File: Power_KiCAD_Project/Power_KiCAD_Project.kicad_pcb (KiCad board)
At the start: 4 copper layers, 80 x 87.2 mm, 73 parts, among them IC1 STM32L562VET6Q, J1 XT60-M, J2 XT60-M, J3 XT60-M, J4 XT60-M, J5 XT60-M, J6 PJ-102AH, J7 L717SDC37P1ACH4F, Q1 CSD17501Q5A, Q2 BSS84PH6327XTSA2, Q3 CSD17501Q5A, SW1 Reboot, U1 MCP9808_MSOP, U2 MCP9808_MSOP, U3 BQ76920PW, U4 LM2678SX-5.0/NOPB, U5 LM2678SX-3.3/NOPB, Y1 Crystal

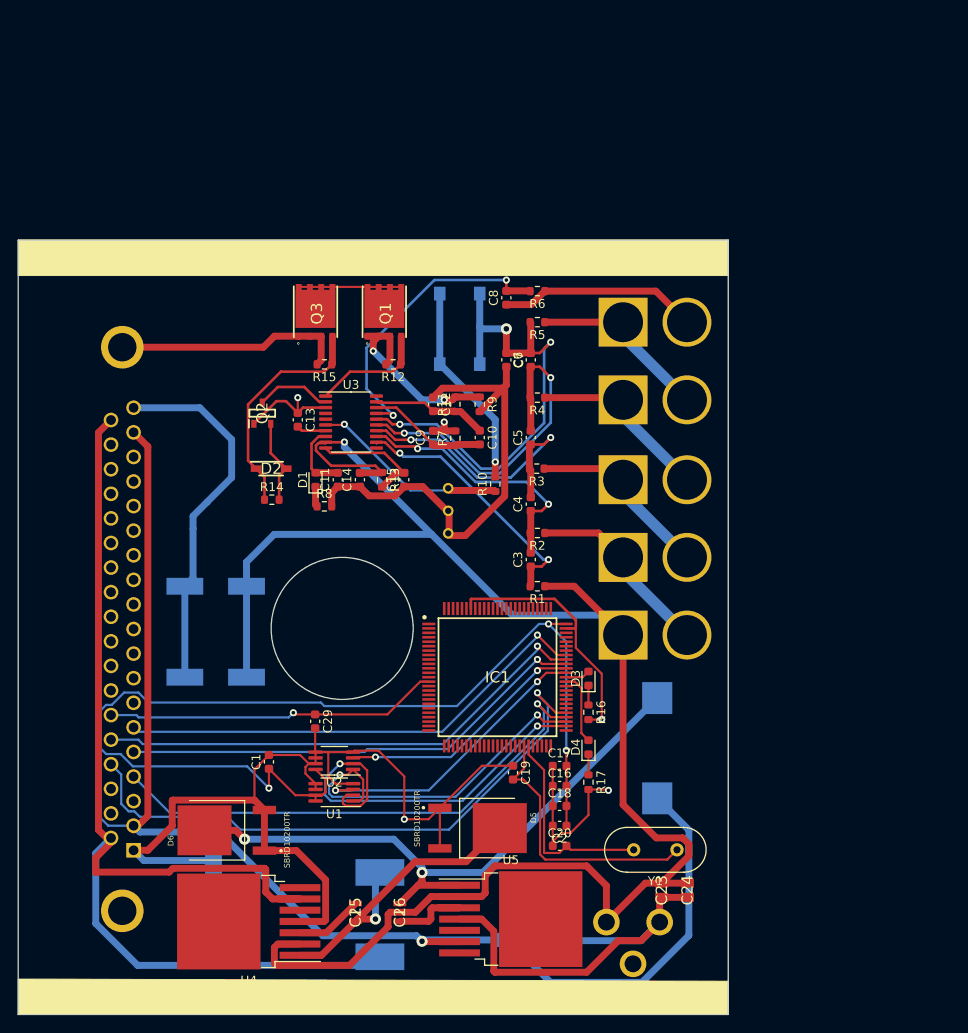
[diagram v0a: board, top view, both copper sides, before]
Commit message: Changes to PCB
re did the pcb and added a "switch"
basically its just an xt60 connector in series with the other ones that needs to be shorted for the board to get power
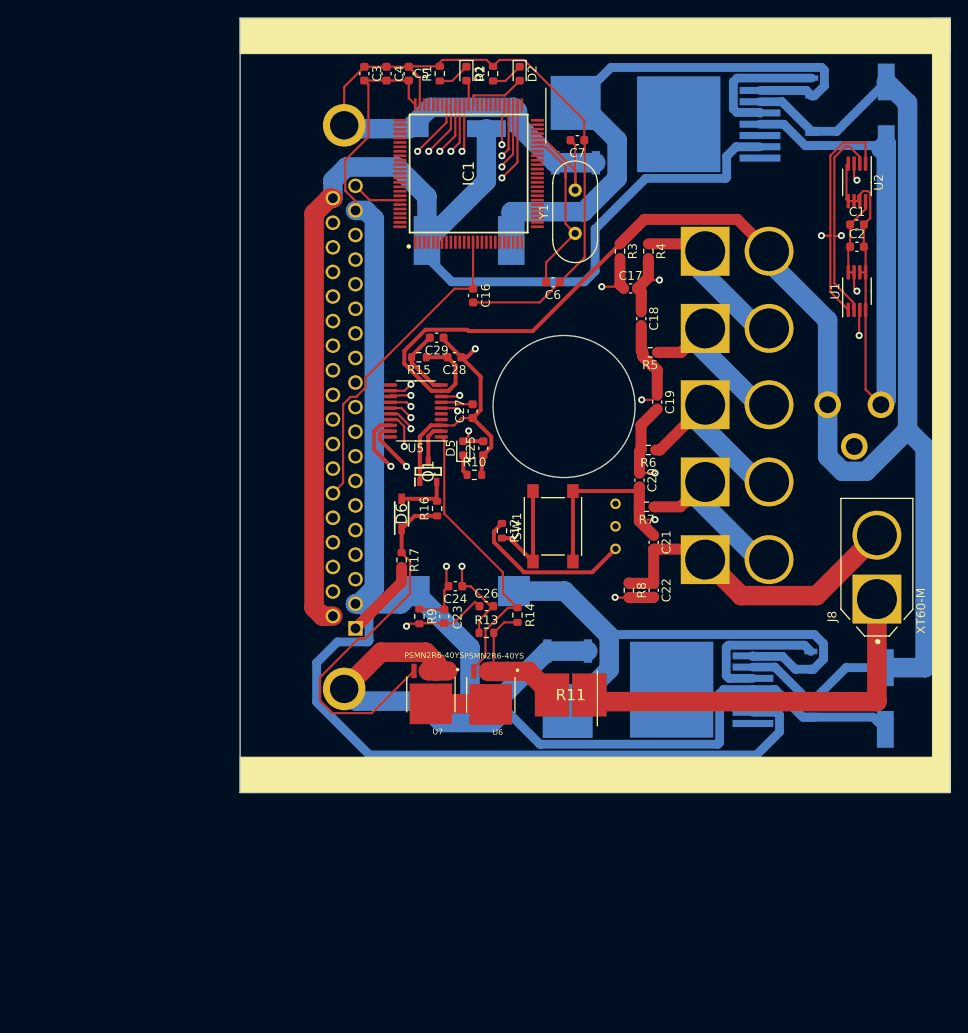
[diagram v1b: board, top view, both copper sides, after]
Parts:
- removed Q2: BSS84PH6327XTSA2, SamacSys_Parts:SOT95P240X110-3N
- removed Q3: CSD17501Q5A, SamacSys_Parts:Q5A
- added J8: XT60-M, XT60-M:AMASS_XT60-M, F.Cu at (171.8, 99.6)
- added U6: PSMN2R6-40YS, TO127P600X120-5N:TO127P600X120-5N, F.Cu at (128.2, 114.0)
- added U7: PSMN2R6-40YS, TO127P600X120-5N:TO127P600X120-5N, F.Cu at (121.5, 113.9)
- C10: value 0.1μF -> C0805C104M5RACTU; footprint Capacitor_SMD:C_0603_1608Metric -> SamacSys_Parts:CAPC2012X88N; moved to B.Cu
- C11: value 4.7μF -> C0805C104M5RACTU; footprint Capacitor_SMD:C_0603_1608Metric -> SamacSys_Parts:CAPC2012X88N; moved to B.Cu
- C12: value 0.1μF -> CGA4C2C0G1H103J060AA; footprint Capacitor_SMD:C_0603_1608Metric -> SamacSys_Parts:CAPC2012X75N; moved to B.Cu
- C13: value 1μF -> CGA4C2C0G1H103J060AA; footprint Capacitor_SMD:C_0603_1608Metric -> SamacSys_Parts:CAPC2012X75N; moved to B.Cu
- C14: value 1μF -> 16SVP330M; footprint Capacitor_SMD:C_0603_1608Metric -> SamacSys_Parts:16SVF1000M; moved to B.Cu
- C15: value 10μF -> 6SVPC330M; footprint Capacitor_SMD:C_0603_1608Metric -> SamacSys_Parts:16SVF180M; moved to B.Cu
- C16: value 1uF -> 100nF
- C17, C18: value 100nF -> 1μF
- C19, C20: value 30pF -> 1μF
- C21, C22: value 35SVPF82M -> 1μF; footprint SamacSys_Parts:16SVPT560M -> Capacitor_SMD:C_0603_1608Metric; moved to F.Cu
- C23, C24: value C0805C104M5RACTU -> 0.1μF; footprint SamacSys_Parts:CAPC2012X88N -> Capacitor_SMD:C_0603_1608Metric
- C25: value CGA4C2C0G1H103J060AA -> 4.7μF; footprint SamacSys_Parts:CAPC2012X75N -> Capacitor_SMD:C_0603_1608Metric
- C26: value CGA4C2C0G1H103J060AA -> 0.1μF; footprint SamacSys_Parts:CAPC2012X75N -> Capacitor_SMD:C_0603_1608Metric
- C27: value 16SVP330M -> 1μF; footprint SamacSys_Parts:16SVF1000M -> Capacitor_SMD:C_0603_1608Metric; moved to F.Cu
- C28: value 6SVPC330M -> 1μF; footprint SamacSys_Parts:16SVF180M -> Capacitor_SMD:C_0603_1608Metric; moved to F.Cu
- C29: value 100nF -> 10μF
- C3: value 1μF -> 1uF
- C4, C5: value 1μF -> 100nF
- C6, C7: value 1μF -> 30pF
- C8: value 1μF -> 35SVPF82M; footprint Capacitor_SMD:C_0603_1608Metric -> SamacSys_Parts:16SVPT560M; moved to B.Cu
- C9: value 0.1μF -> 35SVPF82M; footprint Capacitor_SMD:C_0603_1608Metric -> SamacSys_Parts:16SVPT560M; moved to B.Cu
- D1: value LED -> GREEN
- D2: value 1N4148W-7-F -> RED; footprint SamacSys_Parts:SOD3716X145N -> LED_SMD:LED_0603_1608Metric
- D3: value GREEN -> SBRD10200TR; footprint LED_SMD:LED_0603_1608Metric -> SBRD10200TR:DPAK228P1005X240-4N; moved to B.Cu
- D4: value RED -> SBRD10200TR; footprint LED_SMD:LED_0603_1608Metric -> SBRD10200TR:DPAK228P1005X240-4N; moved to B.Cu
- D5: value SBRD10200TR -> LED; footprint SBRD10200TR:DPAK228P1005X240-4N -> LED_SMD:LED_0603_1608Metric
- D6: value SBRD10200TR -> 1N4148W-7-F; footprint SBRD10200TR:DPAK228P1005X240-4N -> SamacSys_Parts:SOD3716X145N
- Q1: value CSD17501Q5A -> BSS84PH6327XTSA2; footprint SamacSys_Parts:Q5A -> SamacSys_Parts:SOT95P240X110-3N
- R1, R2: value 100Ω -> 1k5Ω
- R10: value 10kΩ -> 1k5Ω
- R11: value 100Ω -> WSHP28185L000FEA; footprint Resistor_SMD:R_0603_1608Metric -> SamacSys_Parts:RESC7146X175N
- R12: value 1MΩ -> 10kΩ
- R15: value 1MΩ -> 100Ω
- R16, R17: value 1k5Ω -> 1MΩ
- R8: value 1k5Ω -> 100Ω
- R9: value .001Ω -> 100Ω
- SW1: moved to F.Cu
- U3: value BQ76920PW -> LM2678SX-5.0/NOPB; footprint Package_SO:TSSOP-20_4.4x6.5mm_P0.65mm -> Package_TO_SOT_SMD:TO-263-7_TabPin8; moved to B.Cu
- U4: value LM2678SX-5.0/NOPB -> LM2678SX-3.3/NOPB; moved to B.Cu
- U5: value LM2678SX-3.3/NOPB -> BQ76920PW; footprint Package_TO_SOT_SMD:TO-263-7_TabPin8 -> Package_SO:TSSOP-20_4.4x6.5mm_P0.65mm
- moved C1 89.7 mm to (169.5, 61.0), turned to 0 degrees
- moved U2 87.8 mm to (169.5, 56.2), turned to 270 degrees
- moved U1 81.6 mm to (169.5, 68.5), turned to 90 degrees
- moved L2 76.6 mm to (125.8, 62.8), turned to 90 degrees
- moved C2 73.3 mm to (169.5, 63.5), turned to 0 degrees
- moved Y1 70.4 mm to (137.8, 62.0), turned to 90 degrees
- moved C28 66.2 mm to (124.2, 76.0), turned to 180 degrees
- moved C13 63.8 mm to (164.3, 110.1)
- moved J6 63.4 mm to (169.2, 85.6)
- moved D3 62.4 mm to (137.8, 49.8), turned to 180 degrees
- moved C27 62.2 mm to (126.2, 82.0), turned to 90 degrees
- moved C11 59.3 mm to (164.3, 115.7), turned to 270 degrees
- moved C9 58.8 mm to (172.7, 114.4), turned to 270 degrees
- moved R1 58.8 mm to (122.5, 44.0), turned to 90 degrees
- moved U5 58.2 mm to (119.8, 82.0), turned to 180 degrees
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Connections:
- C10 pad 1: /LiPo Pack Monitor/SRN -> /PACK_M5
- C10 pad 2: /LiPo Pack Monitor/SRP -> /Pack-
- C11 pad 1: GND -> /PACK_M5
- C11 pad 2: Net-(C11-Pad2) -> /Pack-
- C12 pad 1: GND -> Net-(C12-Pad1)
- C12 pad 2: /LiPo Pack Monitor/SRN -> Net-(C12-Pad2)
- C13 pad 1: GND -> Net-(C13-Pad1)
- C14 pad 1: GND -> +5V
- C14 pad 2: /PACK_M5 -> /Pack-
- C15 pad 1: GND -> +3V3
- C15 pad 2: /LiPo Pack Monitor/BAT -> /Pack-
- C16 pad 1: /Pack- -> /NRST
- C16 pad 2: +3V3 -> /Pack-
- C17 pad 1: /Pack- -> /LiPo Pack Monitor/VC5
- C17 pad 2: +3V3 -> /LiPo Pack Monitor/VC4
- C18 pad 1: /Pack- -> /LiPo Pack Monitor/VC4
- C18 pad 2: +3V3 -> /LiPo Pack Monitor/VC3
- C19 pad 1: /Pack- -> /LiPo Pack Monitor/VC3
- C19 pad 2: Net-(C19-Pad2) -> /LiPo Pack Monitor/VC2
- C20 pad 1: /Pack- -> /LiPo Pack Monitor/VC2
- C20 pad 2: Net-(C20-Pad2) -> /LiPo Pack Monitor/VC1
- C21 pad 1: /PACK_M5 -> /LiPo Pack Monitor/VC1
- C21 pad 2: /Pack- -> GND
- C22 pad 1: /PACK_M5 -> GND
- C22 pad 2: /Pack- -> /LiPo Pack Monitor/VC0
- C23 pad 1: /PACK_M5 -> /LiPo Pack Monitor/SRP
- C23 pad 2: /Pack- -> GND
- C24 pad 1: /PACK_M5 -> /LiPo Pack Monitor/SRN
- C24 pad 2: /Pack- -> /LiPo Pack Monitor/SRP
- C25 pad 1: Net-(C25-Pad1) -> GND
- C26 pad 1: Net-(C26-Pad1) -> GND
- C26 pad 2: Net-(C26-Pad2) -> /LiPo Pack Monitor/SRN
- C27 pad 1: +5V -> GND
- C27 pad 2: /Pack- -> Net-(C27-Pad2)
- C28 pad 1: +3V3 -> GND
- C28 pad 2: /Pack- -> /PACK_M5
- C29 pad 1: /NRST -> GND
- C29 pad 2: /Pack- -> /LiPo Pack Monitor/BAT
- C3 pad 1: /LiPo Pack Monitor/VC5 -> /Pack-
- C3 pad 2: /LiPo Pack Monitor/VC4 -> +3V3
- C4 pad 1: /LiPo Pack Monitor/VC4 -> /Pack-
- C4 pad 2: /LiPo Pack Monitor/VC3 -> +3V3
- C5 pad 1: /LiPo Pack Monitor/VC3 -> /Pack-
- C5 pad 2: /LiPo Pack Monitor/VC2 -> +3V3
- C6 pad 1: /LiPo Pack Monitor/VC2 -> /Pack-
- C6 pad 2: /LiPo Pack Monitor/VC1 -> Net-(C6-Pad2)
- C7 pad 1: /LiPo Pack Monitor/VC1 -> /Pack-
- C7 pad 2: GND -> Net-(C7-Pad2)
- C8 pad 1: GND -> /PACK_M5
- C8 pad 2: /LiPo Pack Monitor/VC0 -> /Pack-
- C9 pad 1: /LiPo Pack Monitor/SRP -> /PACK_M5
- C9 pad 2: GND -> /Pack-
- D1 pad 2: Net-(C11-Pad2) -> Net-(D1-Pad2)
- D3 pad 1: Net-(D3-Pad1) -> /Pack-
- D3 pad 2: Net-(D3-Pad2) -> Net-(C12-Pad2)
- D4 pad 1: Net-(D4-Pad1) -> /Pack-
- D4 pad 2: Net-(D4-Pad2) -> Net-(C13-Pad2)
- D5 pad 1: /Pack- -> Net-(D5-Pad1)
- D6 pad 1: /Pack- -> Net-(D6-Pad1)
- D6 pad 2: Net-(C26-Pad2) -> Net-(D6-Pad2)
- IC1 pad 1: Net-(IC1-Pad1) -> (no net)
- IC1 pad 10: Net-(IC1-Pad10) -> (no net)
- IC1 pad 100: Net-(IC1-Pad100) -> (no net)
- IC1 pad 11: Net-(IC1-Pad11) -> (no net)
- IC1 pad 12: Net-(IC1-Pad12) -> (no net)
- IC1 pad 13: Net-(IC1-Pad13) -> (no net)
- IC1 pad 15: Net-(IC1-Pad15) -> (no net)
- IC1 pad 16: Net-(IC1-Pad16) -> (no net)
- IC1 pad 17: Net-(IC1-Pad17) -> (no net)
- IC1 pad 18: Net-(IC1-Pad18) -> (no net)
- IC1 pad 19: Net-(IC1-Pad19) -> (no net)
- IC1 pad 2: Net-(IC1-Pad2) -> (no net)
- IC1 pad 20: Net-(IC1-Pad20) -> (no net)
- IC1 pad 21: Net-(IC1-Pad21) -> (no net)
- IC1 pad 22: Net-(IC1-Pad22) -> (no net)
- IC1 pad 23: Net-(IC1-Pad23) -> (no net)
- IC1 pad 24: Net-(IC1-Pad24) -> (no net)
- IC1 pad 25: Net-(IC1-Pad25) -> (no net)
- IC1 pad 26: Net-(IC1-Pad26) -> (no net)
- IC1 pad 27: Net-(IC1-Pad27) -> (no net)
- IC1 pad 28: Net-(IC1-Pad28) -> (no net)
- IC1 pad 29: Net-(IC1-Pad29) -> (no net)
- IC1 pad 3: Net-(IC1-Pad3) -> (no net)
- IC1 pad 30: Net-(IC1-Pad30) -> (no net)
- IC1 pad 31: Net-(IC1-Pad31) -> (no net)
- IC1 pad 32: Net-(IC1-Pad32) -> (no net)
- IC1 pad 33: Net-(IC1-Pad33) -> (no net)
- IC1 pad 34: Net-(IC1-Pad34) -> (no net)
- IC1 pad 35: Net-(IC1-Pad35) -> (no net)
- IC1 pad 36: Net-(IC1-Pad36) -> (no net)
- IC1 pad 37: Net-(IC1-Pad37) -> (no net)
- IC1 pad 38: Net-(IC1-Pad38) -> (no net)
- IC1 pad 39: Net-(IC1-Pad39) -> (no net)
- IC1 pad 4: Net-(IC1-Pad4) -> (no net)
- IC1 pad 40: Net-(IC1-Pad40) -> (no net)
- IC1 pad 41: Net-(IC1-Pad41) -> (no net)
- IC1 pad 42: Net-(IC1-Pad42) -> (no net)
- IC1 pad 43: Net-(IC1-Pad43) -> (no net)
- IC1 pad 44: Net-(C19-Pad2) -> Net-(C6-Pad2)
- IC1 pad 45: Net-(C20-Pad2) -> Net-(C7-Pad2)
- IC1 pad 46: Net-(IC1-Pad46) -> (no net)
- IC1 pad 47: Net-(IC1-Pad47) -> (no net)
- IC1 pad 48: Net-(IC1-Pad48) -> (no net)
- IC1 pad 49: Net-(IC1-Pad49) -> (no net)
- IC1 pad 5: Net-(IC1-Pad5) -> (no net)
- IC1 pad 50: Net-(IC1-Pad50) -> (no net)
- IC1 pad 51: Net-(IC1-Pad51) -> (no net)
- IC1 pad 56: Net-(IC1-Pad56) -> (no net)
- IC1 pad 57: Net-(IC1-Pad57) -> (no net)
- IC1 pad 58: Net-(IC1-Pad58) -> (no net)
- IC1 pad 59: Net-(IC1-Pad59) -> (no net)
- IC1 pad 6: Net-(IC1-Pad6) -> (no net)
- IC1 pad 60: Net-(IC1-Pad60) -> (no net)
- IC1 pad 61: Net-(IC1-Pad61) -> (no net)
- IC1 pad 62: Net-(D4-Pad2) -> Net-(D2-Pad2)
- IC1 pad 63: Net-(D3-Pad2) -> Net-(D1-Pad2)
- IC1 pad 69: Net-(IC1-Pad69) -> (no net)
- IC1 pad 7: Net-(IC1-Pad7) -> (no net)
- IC1 pad 70: Net-(IC1-Pad70) -> (no net)
- IC1 pad 71: Net-(IC1-Pad71) -> (no net)
- IC1 pad 72: Net-(IC1-Pad72) -> (no net)
- IC1 pad 73: Net-(IC1-Pad73) -> (no net)
- IC1 pad 76: Net-(IC1-Pad76) -> (no net)
- IC1 pad 77: Net-(IC1-Pad77) -> (no net)
- IC1 pad 78: Net-(IC1-Pad78) -> (no net)
- IC1 pad 79: Net-(IC1-Pad79) -> (no net)
- IC1 pad 8: Net-(IC1-Pad8) -> (no net)
- IC1 pad 80: Net-(IC1-Pad80) -> (no net)
- IC1 pad 81: Net-(IC1-Pad81) -> (no net)
- IC1 pad 82: Net-(IC1-Pad82) -> (no net)
- IC1 pad 83: Net-(IC1-Pad83) -> (no net)
- IC1 pad 84: Net-(IC1-Pad84) -> (no net)
- IC1 pad 85: Net-(IC1-Pad85) -> (no net)
- IC1 pad 86: Net-(IC1-Pad86) -> (no net)
- IC1 pad 87: Net-(IC1-Pad87) -> (no net)
- IC1 pad 88: Net-(IC1-Pad88) -> (no net)
- IC1 pad 89: Net-(IC1-Pad89) -> (no net)
- IC1 pad 9: Net-(IC1-Pad9) -> (no net)
- IC1 pad 90: Net-(IC1-Pad90) -> (no net)
- IC1 pad 91: Net-(IC1-Pad91) -> (no net)
- IC1 pad 92: Net-(IC1-Pad92) -> (no net)
- IC1 pad 93: Net-(IC1-Pad93) -> (no net)
- IC1 pad 95: Net-(IC1-Pad95) -> (no net)
- IC1 pad 96: Net-(IC1-Pad96) -> (no net)
- IC1 pad 97: Net-(IC1-Pad97) -> (no net)
- IC1 pad 98: Net-(IC1-Pad98) -> (no net)
- IC1 pad 99: Net-(IC1-Pad99) -> (no net)
- J1 pad 1: /PACK_M5 -> /PACK_M4
- J1 pad 2: /PACK_M4 -> /PACK_M5
- J2 pad 1: /PACK_M4 -> /PACK_M3
- J2 pad 2: /PACK_M3 -> /PACK_M4
- J3 pad 1: /PACK_M3 -> /PACK_M2
- J3 pad 2: /PACK_M2 -> /PACK_M3
- J4 pad 1: /PACK_M2 -> /PACK_M1
- J4 pad 2: /PACK_M1 -> /PACK_M2
- J5 pad 1: /PACK_M1 -> GND
- J5 pad 2: GND -> /PACK_M1
- J6 pad 3: Net-(J6-Pad3) -> (no net)
- J7 pad 10: Net-(J7-Pad10) -> (no net)
- J7 pad 11: Net-(J7-Pad11) -> (no net)
- J7 pad 12: Net-(J7-Pad12) -> (no net)
- J7 pad 13: Net-(J7-Pad13) -> (no net)
- J7 pad 14: Net-(J7-Pad14) -> (no net)
- J7 pad 15: Net-(J7-Pad15) -> (no net)
- J7 pad 16: Net-(J7-Pad16) -> (no net)
- J7 pad 17: Net-(J7-Pad17) -> (no net)
- J7 pad 21: /Sheet61D3585D/t_mosi -> (no net)
- J7 pad 22: /Sheet61D3585D/t_clk -> (no net)
- J7 pad 26: /Sheet61D3585D/Fire_redundant -> (no net)
- J7 pad 27: Net-(J7-Pad27) -> (no net)
- J7 pad 28: Net-(J7-Pad28) -> (no net)
- J7 pad 29: Net-(J7-Pad29) -> (no net)
- J7 pad 3: /Sheet61D3585D/t_miso -> (no net)
- J7 pad 30: Net-(J7-Pad30) -> (no net)
- J7 pad 31: Net-(J7-Pad31) -> (no net)
- J7 pad 32: Net-(J7-Pad32) -> (no net)
- J7 pad 33: Net-(J7-Pad33) -> (no net)
- J7 pad 34: Net-(J7-Pad34) -> (no net)
- J7 pad 35: Net-(J7-Pad35) -> (no net)
- J7 pad 36: Net-(J7-Pad36) -> (no net)
- J7 pad 7: /Sheet61D3585D/Fire -> (no net)
- J7 pad 8: Net-(J7-Pad8) -> (no net)
- J7 pad 9: Net-(J7-Pad9) -> (no net)
- L1 pad 1: Net-(C26-Pad2) -> Net-(C13-Pad2)
- L2 pad 1: Net-(C25-Pad2) -> Net-(C12-Pad2)
- Q1 pad 1: Net-(Q1-Pad1) -> GND
- Q1 pad 2: Net-(Q1-Pad1) -> Net-(D6-Pad2)
- Q1 pad 3: Net-(Q1-Pad1) -> Net-(Q1-Pad3)
- R1 pad 1: /PACK_M5 -> Net-(D1-Pad1)
- R1 pad 2: /LiPo Pack Monitor/VC5 -> /Pack-
- R10 pad 1: /LiPo Pack Monitor/TS1 -> Net-(D5-Pad1)
- R10 pad 2: Net-(R10-Pad2) -> GND
- R11 pad 1: /LiPo Pack Monitor/SRN -> GND
- R11 pad 2: Net-(Q1-Pad1) -> Net-(R11-Pad2)
- R12 pad 1: Net-(Q1-Pad4) -> /LiPo Pack Monitor/TS1
- R12 pad 2: Net-(Q1-Pad1) -> Net-(R12-Pad2)
- R13 pad 1: /PACK_M5 -> /LiPo Pack Monitor/SRN
- R13 pad 2: /LiPo Pack Monitor/BAT -> Net-(R11-Pad2)
- R14 pad 1: Net-(D2-Pad1) -> Net-(R14-Pad1)
- R14 pad 2: Net-(D2-Pad2) -> Net-(R11-Pad2)
- R15 pad 1: Net-(D2-Pad1) -> /PACK_M5
- R15 pad 2: /Pack- -> /LiPo Pack Monitor/BAT
- R16 pad 1: Net-(D3-Pad1) -> Net-(D6-Pad1)
- R16 pad 2: /Pack- -> Net-(D6-Pad2)
- R17 pad 1: Net-(D4-Pad1) -> Net-(D6-Pad1)
- R2 pad 1: /PACK_M4 -> Net-(D2-Pad1)
- R2 pad 2: /LiPo Pack Monitor/VC4 -> /Pack-
- R3 pad 1: /PACK_M3 -> /PACK_M5
- R3 pad 2: /LiPo Pack Monitor/VC3 -> /LiPo Pack Monitor/VC5
- R4 pad 1: /PACK_M2 -> /PACK_M4
- R4 pad 2: /LiPo Pack Monitor/VC2 -> /LiPo Pack Monitor/VC4
- R5 pad 1: /PACK_M1 -> /PACK_M3
- R5 pad 2: /LiPo Pack Monitor/VC1 -> /LiPo Pack Monitor/VC3
- R6 pad 1: GND -> /PACK_M2
- R6 pad 2: /LiPo Pack Monitor/VC0 -> /LiPo Pack Monitor/VC2
- R7 pad 1: /LiPo Pack Monitor/SRP -> /PACK_M1
- R7 pad 2: GND -> /LiPo Pack Monitor/VC1
- R8 pad 1: Net-(D1-Pad1) -> GND
- R8 pad 2: GND -> /LiPo Pack Monitor/VC0
- R9 pad 1: Net-(Q1-Pad1) -> /LiPo Pack Monitor/SRP
- SW1 pad 1: Net-(R10-Pad2) -> Net-(R12-Pad2)
- U3 pad 1: Net-(Q1-Pad4) -> Net-(C12-Pad2)
- U3 pad 2: Net-(Q2-Pad3) -> /PACK_M5
- U3 pad 3: GND -> Net-(C12-Pad1)
- U3 pad 4: /LiPo Pack Monitor/I2C_SDA -> /Pack-
- U3 pad 5: /LiPo Pack Monitor/I2C_SCL -> (no net)
- U3 pad 6: /LiPo Pack Monitor/TS1 -> +5V
- U3 pad 7: Net-(C13-Pad2) -> (no net)
- U3 pad 8: Net-(C11-Pad2) -> (no net)
- U4 pad 1: Net-(C25-Pad2) -> Net-(C13-Pad2)
- U4 pad 3: Net-(C25-Pad1) -> Net-(C13-Pad1)
- U4 pad 6: +5V -> +3V3
- U4 pad 7: Net-(U4-Pad7) -> (no net)
- U5 pad 1: Net-(C26-Pad2) -> Net-(R14-Pad1)
- U5 pad 2: /PACK_M5 -> Net-(Q1-Pad3)
- U5 pad 3: Net-(C26-Pad1) -> GND
- U5 pad 4: /Pack- -> (no net)
- U5 pad 6: +3V3 -> /LiPo Pack Monitor/TS1
- U5 pad 7: Net-(U5-Pad7) -> Net-(C27-Pad2)
- U5 pad 8: (no net) -> Net-(C25-Pad2)
- Y1 pad 1: Net-(C19-Pad2) -> Net-(C6-Pad2)
- Y1 pad 2: Net-(C20-Pad2) -> Net-(C7-Pad2)
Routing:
- net Net-(C26-Pad2): track 70.6 -> 0.00 mm, vias 2 -> 0
- net Net-(C12-Pad2): track 0.00 -> 67.0 mm
- net Net-(C13-Pad2): track 3.32 -> 58.7 mm
- net Net-(D6-Pad1): track 0.00 -> 42.1 mm
- net /TEMP_ALERT_1: track 33.5 -> 69.3 mm
- net /I2C_SDA: track 40.3 -> 74.8 mm
- net Net-(R14-Pad1): track 0.00 -> 32.6 mm
- net Net-(C19-Pad2): track 30.8 -> 0.00 mm
- net GND: track 92.8 -> 123.5 mm
- net /TEMP_ALERT_2: track 28.2 -> 56.3 mm
- net /I2C_SCL: track 46.8 -> 73.5 mm
- net Net-(C25-Pad2): track 36.3 -> 10.5 mm, vias 1 -> 2
- net /LiPo Pack Monitor/VC3: track 32.3 -> 57.2 mm
- net /LiPo Pack Monitor/TS1: track 22.3 -> 46.6 mm
- net /Pack-: track 277.0 -> 301.0 mm, vias 3 -> 0
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- added copper zone on ground, net /Pack-
- removed copper zone on ground_2, net /Pack-

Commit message: PCB changes
did some changes to the PCB to make sure that everything is fully isolated.
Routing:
- net GND: track 123.5 -> 125.7 mm
